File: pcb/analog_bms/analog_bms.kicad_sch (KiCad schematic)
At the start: 51 parts, among them J1 Screw_Terminal_01x02, Q1 PMOS, Q2 NMOS, Q3 PMOS, Q4 NMOS, Q5 PMOS, U1 TLV7031DBV, U2 TLV7031DBV, U3 TLV7032QDDFRQ1, U3 TPS7A2401DBVR, U4 TPS7A2401DBVR, U5 LTC1754

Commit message: Printable 18650 + Mounting Hole
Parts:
- removed J1: Screw_Terminal_01x02, symbol Connector:Screw_Terminal_01x02
- added H1: ~, analog_bms_library:M3_Mounting_Through_Hole, symbol analog_bms_library:M3_Mounting_Through_Hole
- added J1: Screw_Terminal_1x2, analog_bms_library:691502710002, symbol analog_bms_library:691502710002
- added J2: MODULE+, TestPoint:TestPoint_THTPad_D3.0mm_Drill1.5mm, symbol Connector:Conn_01x01_Pin
- added J3: MODULE-, TestPoint:TestPoint_THTPad_D3.0mm_Drill1.5mm, symbol Connector:Conn_01x01_Pin
- added R30: 1M, Resistor_SMD:R_0805_2012Metric, symbol Device:R
- C1, C2, C3, C4, C5: footprint (none) -> Capacitor_SMD:C_0805_2012Metric
- D1, D2, D3, D4: footprint (none) -> Diode_SMD:D_SOD-323
- F1: footprint analog_bms_library:TLV7032QDDFRQ1 -> Resistor_SMD:R_0805_2012Metric
- Q1, Q2, Q3, Q4, Q5: footprint (none) -> Package_TO_SOT_SMD:TSOT-23
- R10, R11, R12, R13, R14, R15, R16, R17, R18, R19, R2, R20, R21, R22, R23, R24, R25, R26, R27, R28, R29, R3, R6, R7, R8, R9: footprint (none) -> Resistor_SMD:R_0805_2012Metric
- R4: value 50k -> 100k; footprint (none) -> Resistor_SMD:R_0805_2012Metric
- R5: value R -> 100k; footprint (none) -> Resistor_SMD:R_0805_2012Metric; now fitted
- U4: renamed from U3; footprint analog_bms_library:TLV7032QDDFRQ1 -> analog_bms_library:SOT95P280X145-5N
- U5: renamed from U4; footprint analog_bms_library:TLV7032QDDFRQ1 -> analog_bms_library:SOT95P280X145-5N
- renumbered U5 to U6
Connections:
- net +BATT: now also R30.2; no longer R17.2
- net +MODULE: now also J2.1 (Pin_1)
- net -MODULE: now also R17.2, J1.2, J3.1 (Pin_1)
- net at Q4.1 (D): now also J1.1; no longer Q3.1 (D)
- net at Q4.2 (G), Q5.1 (D): now also R30.1
- net at Q4.3 (S): now also Q3.1 (D)
- net at Q2.1 (D): now also Q3.3 (S); no longer Q1.1 (D)
- net at Q2.3 (S): now also Q1.1 (D); no longer Q3.3 (S)
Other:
- title: (none) -> Analog BMS
- moved on the sheet: Q2, Q4, Q5

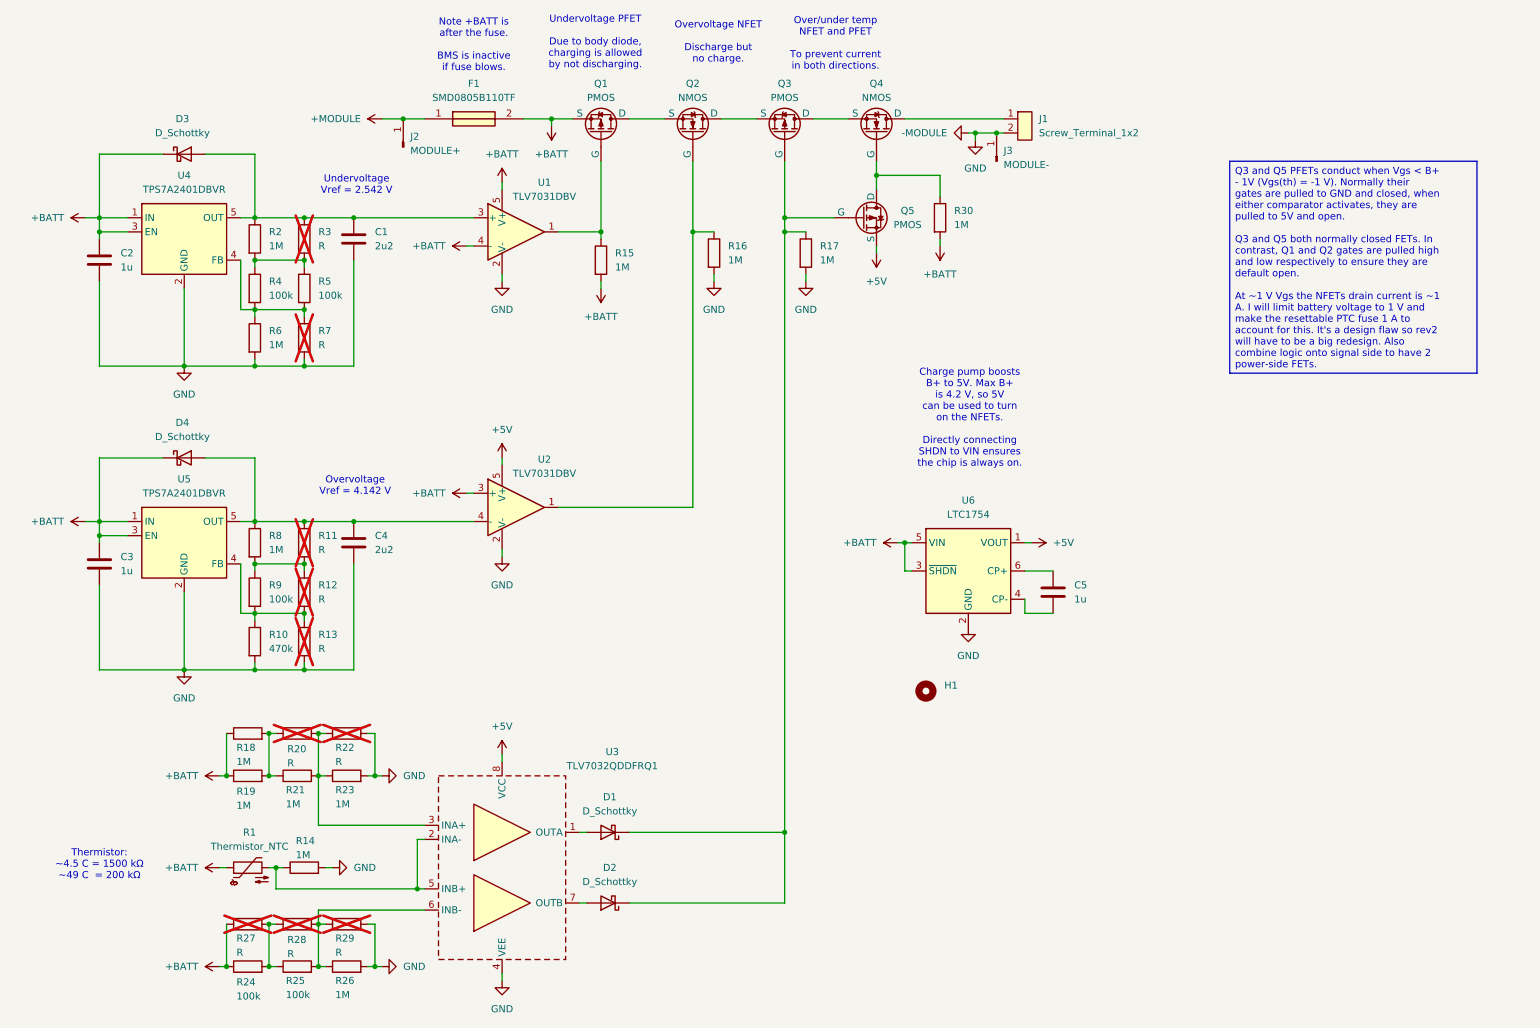
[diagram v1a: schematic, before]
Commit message: PCB Design Complete - Pass DRC
Still skeptical of the DRC. Some very close silk screen elements.
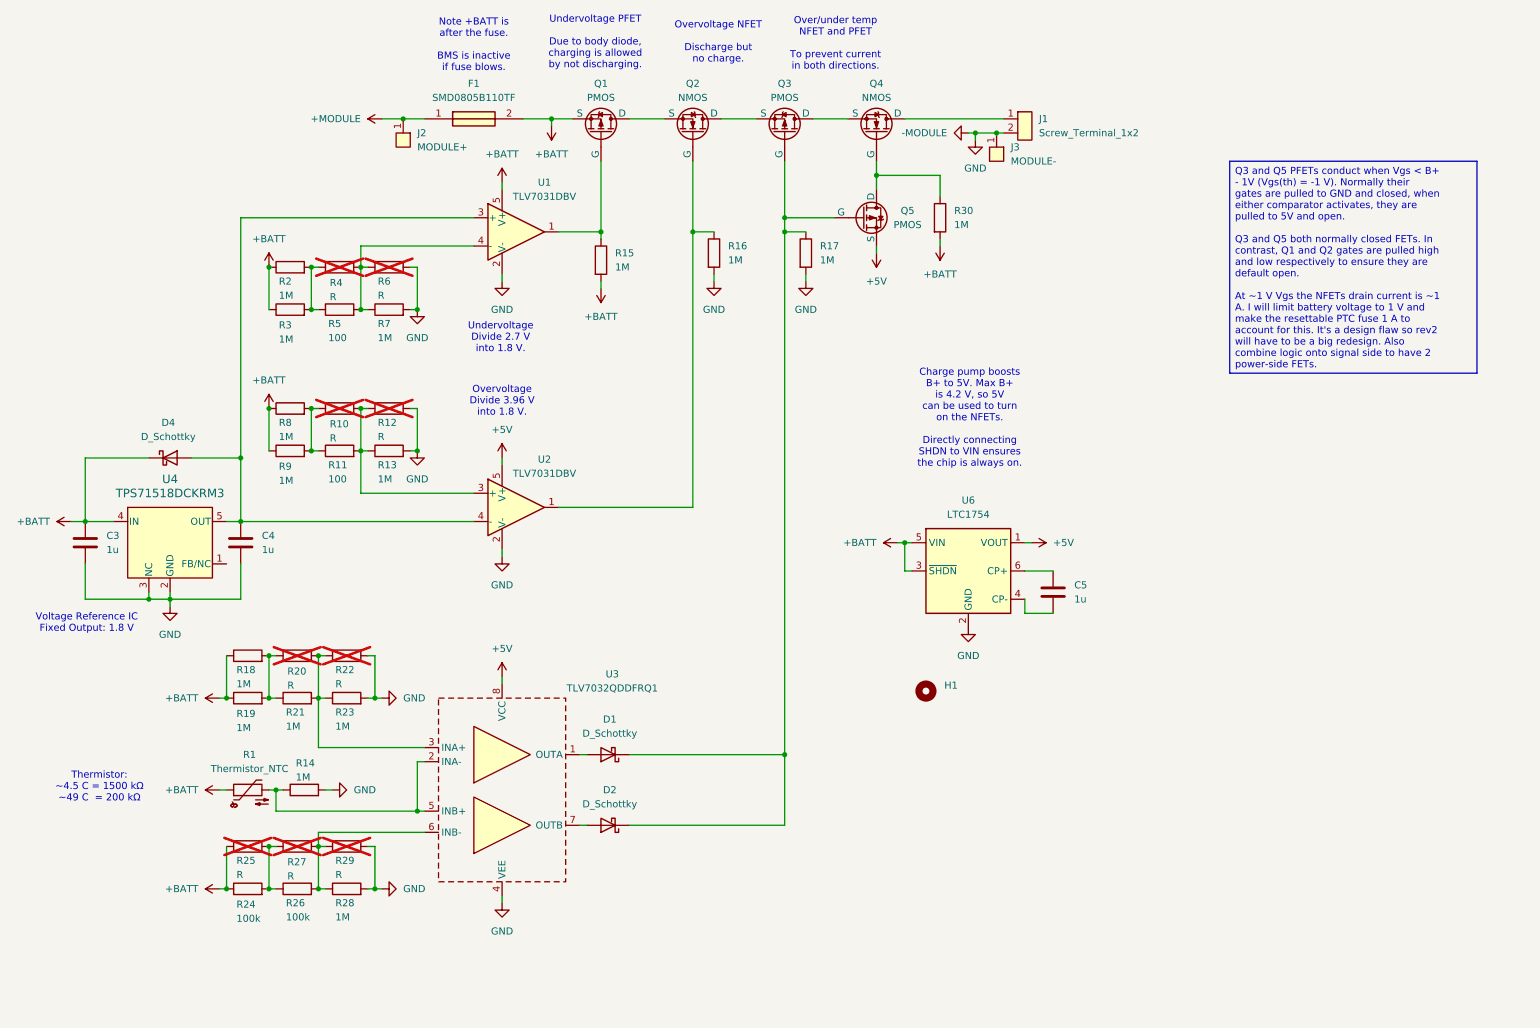
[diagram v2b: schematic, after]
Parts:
- removed C1: 2u2, Capacitor_SMD:C_0805_2012Metric, symbol Device:C
- removed C2: 1u, Capacitor_SMD:C_0805_2012Metric, symbol Device:C
- removed D3: D_Schottky, Diode_SMD:D_SOD-323, symbol Device:D_Schottky
- removed J2: MODULE+, TestPoint:TestPoint_THTPad_D3.0mm_Drill1.5mm, symbol Connector:Conn_01x01_Pin
- removed J3: MODULE-, TestPoint:TestPoint_THTPad_D3.0mm_Drill1.5mm, symbol Connector:Conn_01x01_Pin
- removed U4, U5: TPS7A2401DBVR, analog_bms_library:SOT95P280X145-5N, symbol analog_bms_library:TPS7A2401DBVR
- added J2: MODULE+, analog_bms_library:1.5_mm_Through_Hole, symbol analog_bms_library:1.5_mm_Through_Hole
- added J3: MODULE-, analog_bms_library:1.5_mm_Through_Hole, symbol analog_bms_library:1.5_mm_Through_Hole
- added U4: TPS71518DCKRM3, analog_bms_library:TPS71518DCKRM3, symbol analog_bms_library:TPS71518DCKRM3
- C4: value 2u2 -> 1u
- Q1, Q2, Q3, Q4, Q5: footprint Package_TO_SOT_SMD:TSOT-23 -> analog_bms_library:TSOT_23_No_Arrow
- R10: value 470k -> R; now not fitted
- R11: value R -> 100; now fitted
- R13, R3, R7: value R -> 1M; now fitted
- R4: value 100k -> R; now not fitted
- R5: value 100k -> 100
- R6: value 1M -> R; now not fitted
- R9: value 100k -> 1M
- renumbered R27 to R25, R25 to R26, R28 to R27, R26 to R28
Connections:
- net +BATT: now also R2.1, R3.1, R8.1, R9.1, U4.4 (IN); no longer U1.4 (-), U2.3 (+)
- net +MODULE: now also J2.1
- net -MODULE: now also R12.2, J3.1, U4.2 (GND), U4.3 (NC); no longer R10.2
- net at R10.1, R9.2: now also R11.1, R8.2; no longer R12.2, R13.1
- net at C4.1, D4.2 (A), U2.4 (-): now also U1.3 (+), U4.5 (OUT); no longer R11.1, R8.1
- net at R4.2, R5.2, R6.1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: now also U1.4 (-)
- net at R11.2, R12.1: now also R10.2, R13.1, U2.3 (+); no longer R8.2, R9.1
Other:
- note added: "Overvoltage Divide 3.96 V into 1.8 V."
- note added: "Undervoltage Divide 2.7 V into 1.8 V."
- note added: "Voltage Reference IC Fixed Output: 1.8 V"
- note removed: "Overvoltage Vref = 4.142 V"
- note removed: "Undervoltage Vref = 2.542 V"
- moved on the sheet: C3, D1, D2, D4, R1, R14, R18, R19, R20, R21, R22, R23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

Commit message: Black PCB + Renders
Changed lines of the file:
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@@
 	(text_box "Q3 and Q5 PFETs conduct when Vgs < B+ - 1V (Vgs(th) = -1 V). Normally their gates are pulled to GND and closed, when either comparator activates, they are pulled to 5V and open.\n\nQ3 and Q5 both normally closed FETs. In contrast, Q1 and Q2 gates are pulled high and low respectively to ensure they are default open.\n\nAt ~1 V Vgs the NFETs drain current is ~1 A. I will limit battery voltage to 1 V and make the resettable PTC fuse 1 A to account for this. It's a design flaw so rev2 will have to be a big redesign. Also combine logic onto signal side to have 2 power-side FETs."
 		(exclude_from_sim no)
-		(at 231.14 39.37 0)
+		(at 209.55 49.53 0)
 		(size 44.45 38.1)
 		(margins 0.9525 0.9525 0.9525 0.9525)
